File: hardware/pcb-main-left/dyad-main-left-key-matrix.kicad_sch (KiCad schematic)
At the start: 65 parts, among them SW1 SW_Push, SW10 SW_Push, SW11 SW_Push, SW12 SW_Push, SW13 SW_Push, SW14 SW_Push, SW15 SW_Push, SW16 SW_Push, SW17 SW_Push, SW18 SW_Push, SW19 SW_Push, SW2 SW_Push, SW20 SW_Push, SW21 SW_Push, SW22 SW_Push, SW23 SW_Push, SW24 SW_Push, SW25 SW_Push, SW26 SW_Push, SW27 SW_Push, SW28 SW_Push, SW29 SW_Push, SW3 SW_Push, SW30 SW_Push, SW31 SW_Push, SW32 SW_Push, SW4 SW_Push, SW5 SW_Push, SW6 SW_Push, SW7 SW_Push, SW8 SW_Push, SW9 SW_Push

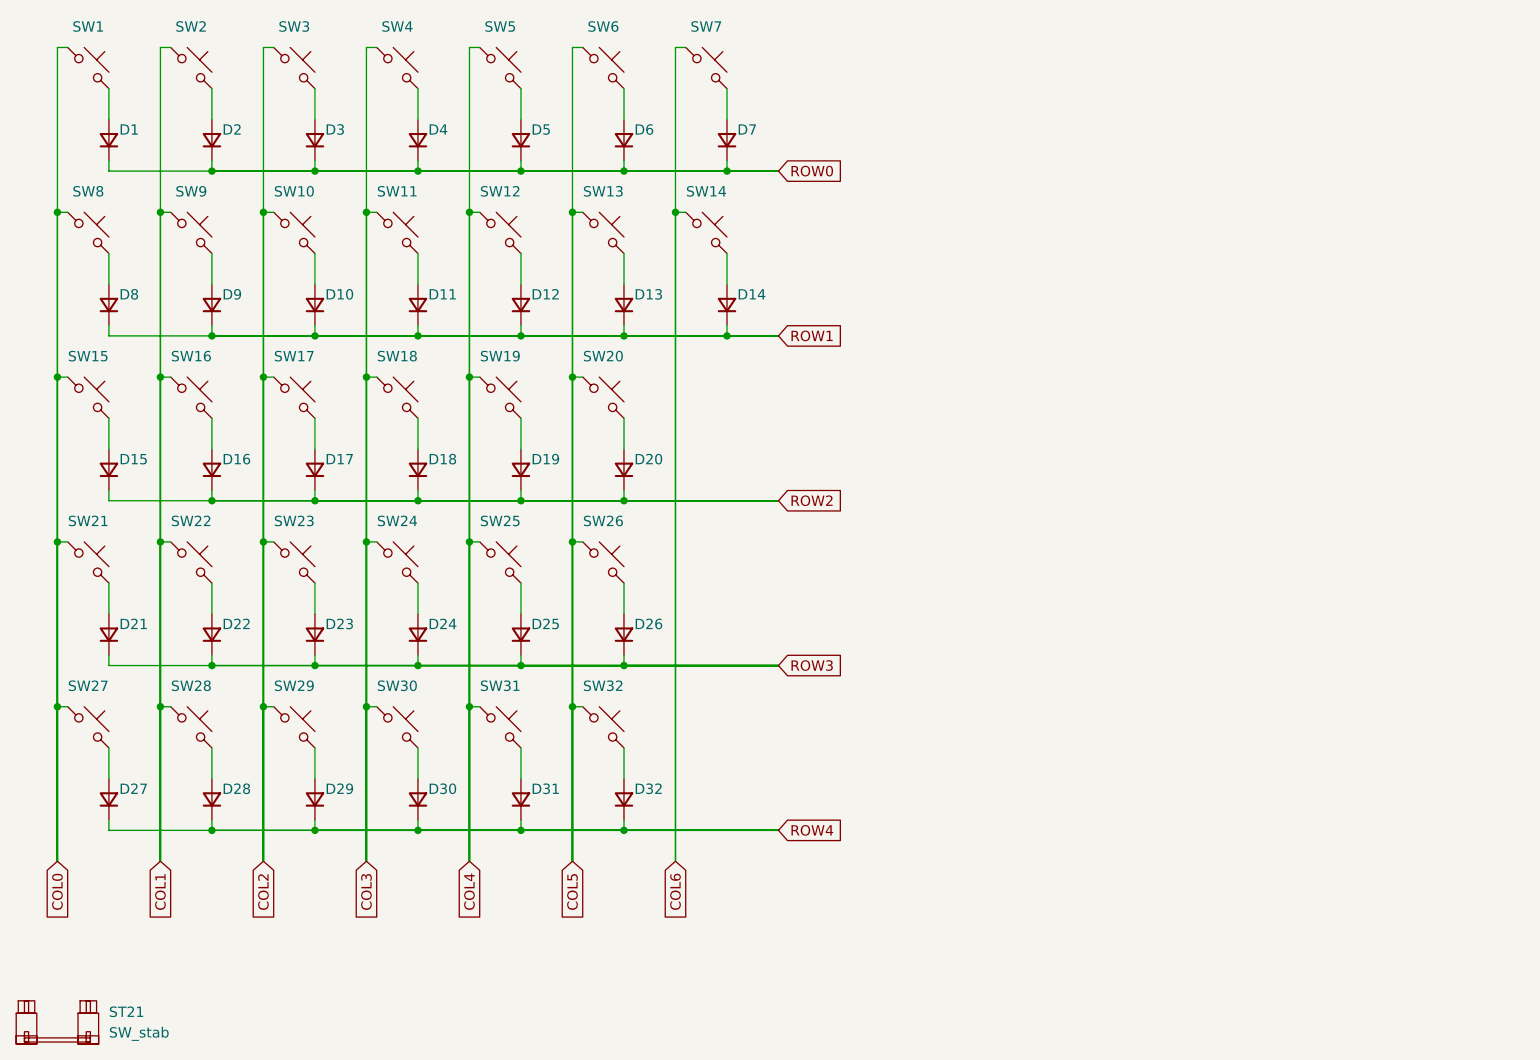
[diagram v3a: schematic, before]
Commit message: Left half fully routed, and repair a dragged board-outline corner
330 segments and 32 vias close every connection on main-left. Unconnected
125 -> 0, schematic parity 98 -> 0, no shorts.

Routing also caught a board-outline break that DRC reported as three
invalid_outline errors -- "Board has malformed outline (not a closed shape)".
Nothing was deleted: a three-segment rounded corner had been dragged by
exactly (-6.137, -4.900) mm, leaving a 2.85 mm gap where it belonged and a
dangling spur where it landed. Segment count stayed at 23 either way, which
is why it was not obvious; the tell was four Edge.Cuts endpoints used once
instead of zero.

Restored the three segments to their committed coordinates, then refilled
both pours -- they had been filled against the displaced edge and sat at
0.0000 mm from the restored one, which surfaced as two copper_edge_clearance
errors in between.

  invalid_outline        3 -> 0
  copper_edge_clearance  0 -> 2 -> 0
  Edge.Cuts open ends    4 -> 0

Both halves now carry only cosmetic silkscreen warnings and the deliberate
D/SW courtyard overlaps:

              violations  errors  unconnected  parity  shorts
  main-left          195      32            0       0       0
  main-right         253      37            0       0       0

Co-Authored-By: Claude Opus 5 <noreply@anthropic.com>
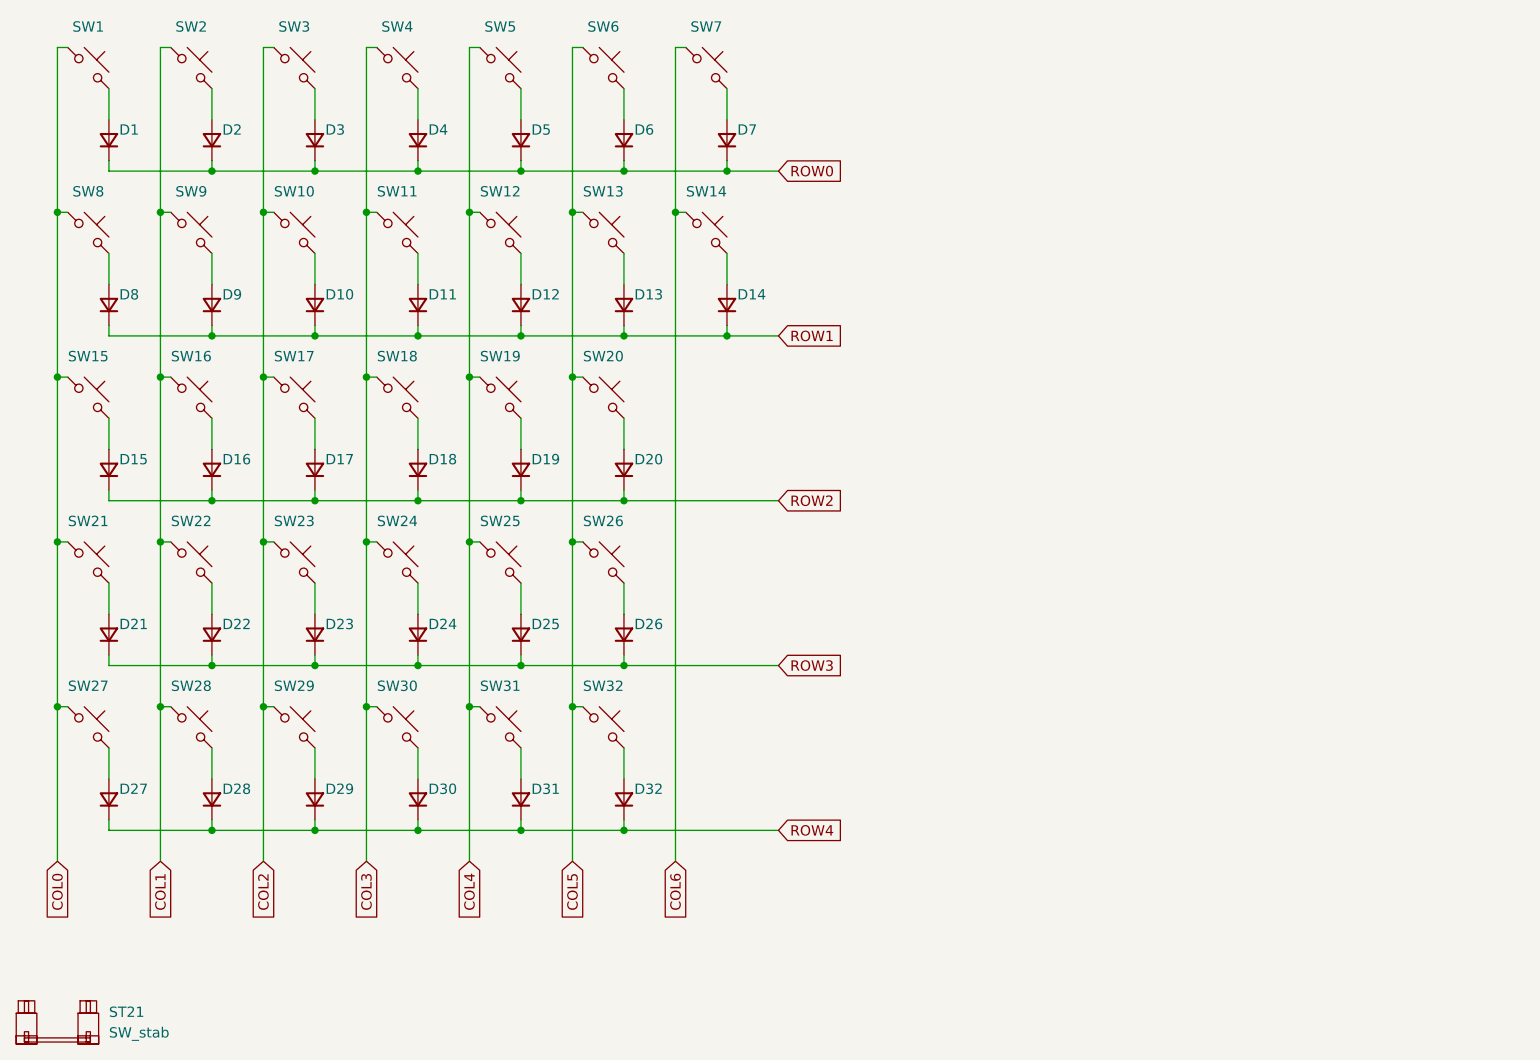
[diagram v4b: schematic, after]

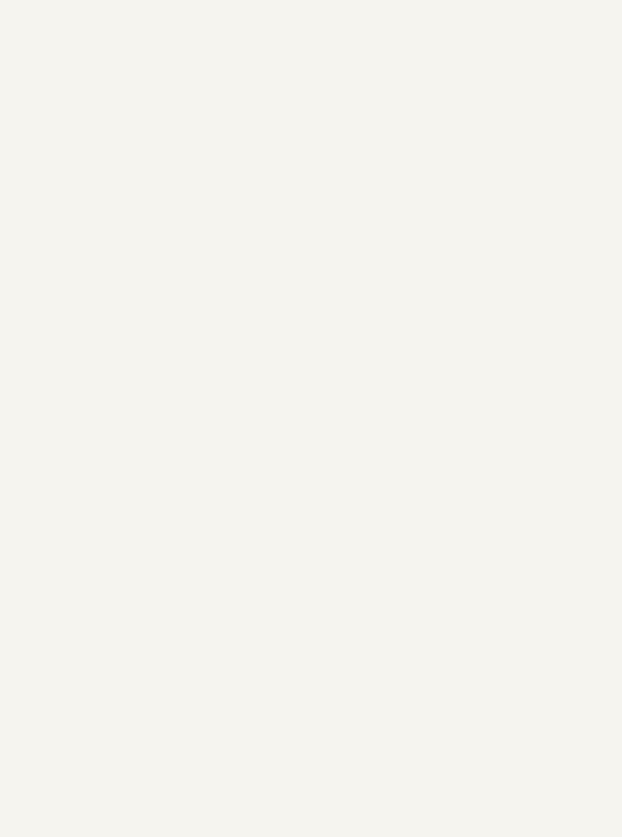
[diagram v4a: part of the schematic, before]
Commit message: Add the 20-pin FFC connector to the left half's schematic
J1 in the key-matrix sheet, same symbol and same C19273932 footprint as
main-right, all 20 lines wired, and the `dyad` library registered in
main-left's fp-lib-table with the same relative URI.

Wired identically to main-right, including the descending rows. Two things
the left half forces to differ:

  Handedness ties to +3V3 rather than GND, so pins 19 and 20 are the same
  net here and are bussed under one +3V3 symbol. On the right they are two.

  Pin 18 is idle -- the left half has only COL0-6, as PLAN.md specifies. It
  is labelled COL7 rather than no-connected, so the cable line stays
  documented and an eighth column stays wireable. The cost is one
  isolated_pin_label warning, the same accepted class as LEDOUT.

ERC errors 3 -> 0, violations 116 -> 113: both power_pin_not_driven and the
pin_not_driven on LED1 DIN clear, and LEDIN is no longer isolated. The two
remaining isolated_pin_label warnings are COL7 and LEDOUT, both correct by
spec. The 110 endpoint_off_grid warnings are untouched, confirming every
added item is on-grid, and the single lib_symbol_issues warning is
pre-existing.

The pinout is recorded as PROVISIONAL. The left connector faces the other
way, so there is a real question about mirroring it; the doc now works
through why a flip reverses all twenty pins rather than just the rows, why
cable type A/B is the right place to absorb it, and what the QMK escape
hatch costs if routing disagrees. Decision deferred to placement.

Co-Authored-By: Claude Opus 5 <noreply@anthropic.com>
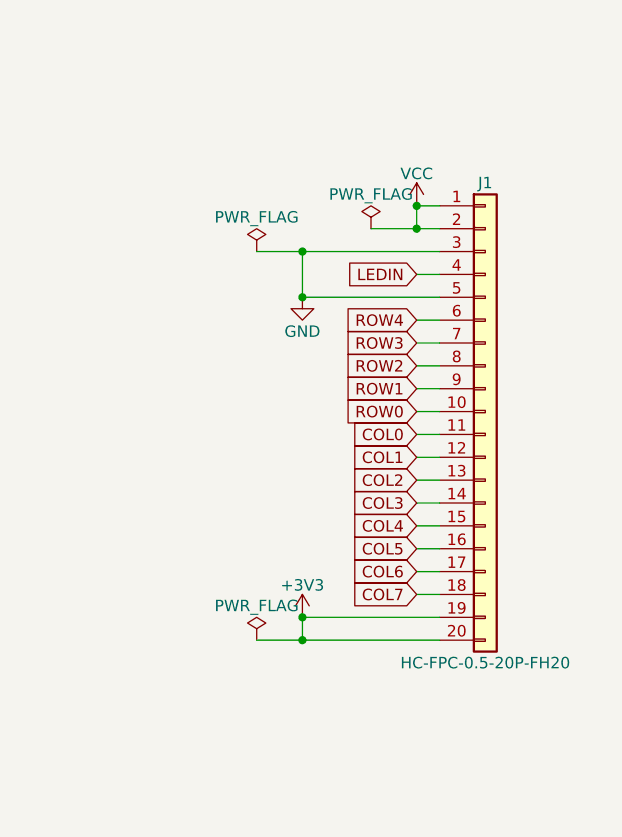
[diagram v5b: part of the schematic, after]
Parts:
- added J1: HC-FPC-0.5-20P-FH20, dyad:FPC-SMD_20P-P0.50_HC-FPC-0.5-20P-FH20, symbol Connector_Generic:Conn_01x20
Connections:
- net COL0: now also J1.11 (Pin_11)
- net COL1: now also J1.12 (Pin_12)
- net COL2: now also J1.13 (Pin_13)
- net COL3: now also J1.14 (Pin_14)
- net COL4: now also J1.15 (Pin_15)
- net COL5: now also J1.16 (Pin_16)
- net COL6: now also J1.17 (Pin_17)
- net ROW0: now also J1.10 (Pin_10)
- net ROW1: now also J1.9 (Pin_9)
- net ROW2: now also J1.8 (Pin_8)
- net ROW3: now also J1.7 (Pin_7)
- net ROW4: now also J1.6 (Pin_6)
- new net +3V3: J1.19 (Pin_19), J1.20 (Pin_20)
- new net COL7: J1.18 (Pin_18)
- new net GND: J1.3 (Pin_3), J1.5 (Pin_5)
- new net LEDIN: J1.4 (Pin_4)
- new net VCC: J1.1 (Pin_1), J1.2 (Pin_2)

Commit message: Put the main FFC on two controller edges, one populated
Each half's J1 sits on its own inner board edge, so the two cable
approaches are mirror images of each other -- and a mirror is not a
rotation. Turning the controller 180 degrees swaps left/right *and*
top/bottom, which would put the main FFC on the right edge but USB-C on the
wrong one. Only flipping the board over truly mirrors it, and that faces
every component at the case floor and inverts the USB-C port.

So the controller carries the 20-pin footprint on two edges, wired to the
same nets, with only the one facing that half's main PCB fitted. Each
footprint's orientation is chosen independently, so the mirror is absorbed
in controller copper.

That is WORKFLOW.md §2 applied literally: push the uncertainty into the part
with the most slack. The controller is named there as having "enormous
slack" at ~$15 to respin; the mains have none, and main-right is already
routed. The project already uses the same unpopulated-footprint pattern for
the SK6812s and the DNP 74AHCT125.

Consequence: main-left's pinout is no longer provisional. Both halves keep
one cable type, one logical pinout and one firmware build, and J1's Pinout
property on main-left drops the PROVISIONAL marker.

Costs recorded for layout: ~13 mm of edge twice, about 53 mm of the ~170 mm
perimeter once both USB-C and the knob FFC are counted, and a stub on all 20
nets -- irrelevant except for LEDIN, the only line with fast edges.

Rejected: folding the cable on one half (cheapest, but assembly-order
dependent and easiest to get silently wrong); relocating both J1s so the
halves relate by translation (would redo main-right's placement and
routing); flipping the controller over.

interface.yaml goes to v11. Its note already required the controller to sit
"somewhere reachable by both FFCs" -- that is now cashed out, and
positions_controller and mounting_holes must additionally record which edge
is populated on each half. The WORKFLOW §7 ritual cannot com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
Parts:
- J1: Pinout PROVISIONAL - confirm at routing. 1,2=VCC(5V) 3,5=GND 4=LED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 -> 1,2=VCC(5V) 3,5=GND 4=LEDIN 6-10=ROW4..ROW0 (descending) 11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
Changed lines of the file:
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@@
 			)
 		)
-		(property "Pinout" "PROVISIONAL - confirm at routing. 1,2=VCC(5V) 3,5=GND 4=LEDIN 6-10=ROW4..ROW0 (descending) 11-17=COL0-6 18=COL7 (idle on left) 19=+3V3 20=HAND(tied to +3V3 here)"
+		(property "Pinout" "1,2=VCC(5V) 3,5=GND 4=LEDIN 6-10=ROW4..ROW0 (descending) 11-17=COL0-6 18=COL7 (idle on left) 19=+3V3 20=HAND(tied to +3V3 here). Identical to main-right; the mirrored approach is absorbed by the controller's second FFC footprint."
 			(at 193.04 66.04 0)
 			(hide yes)
